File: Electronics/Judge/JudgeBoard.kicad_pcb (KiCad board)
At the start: 2 copper layers, 21 parts, among them J1 RJ12-UNSHLD, U1 74HC165, U2 74HC165

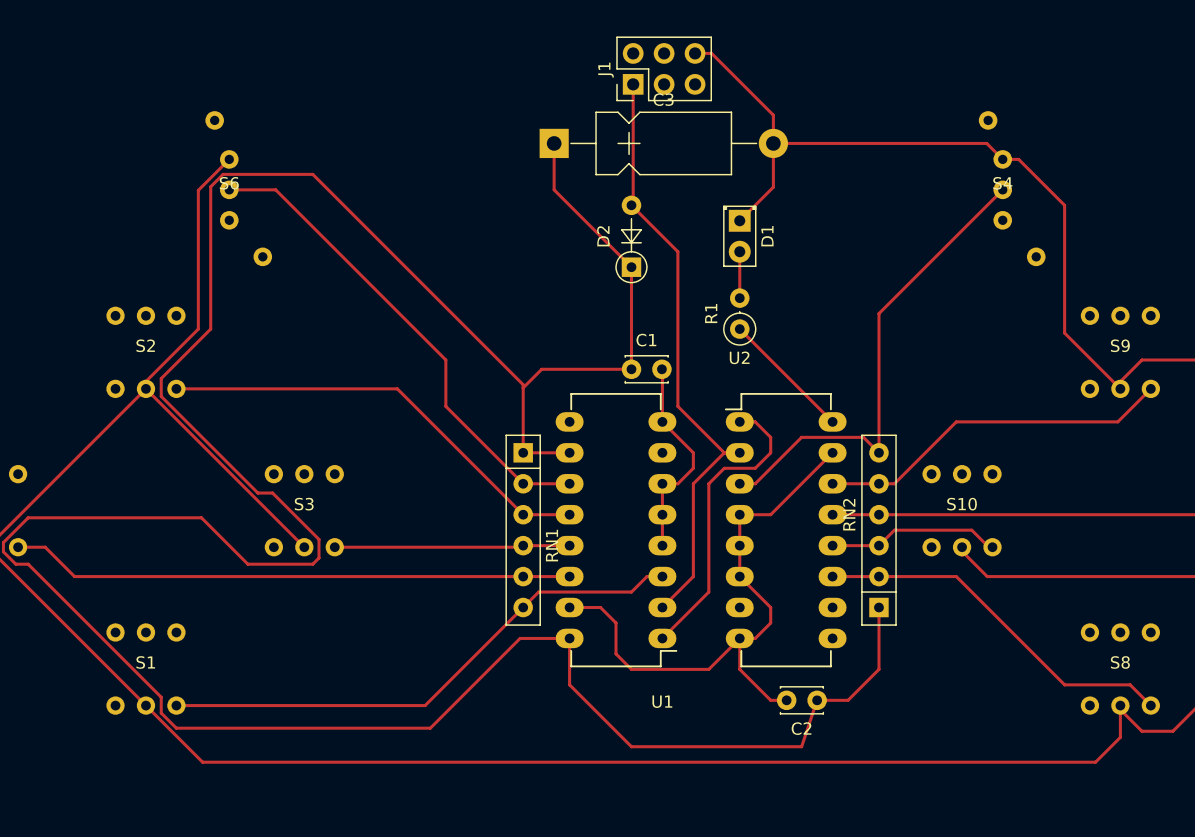
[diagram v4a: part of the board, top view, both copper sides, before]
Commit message: Reduced judge board to 2 jumpers
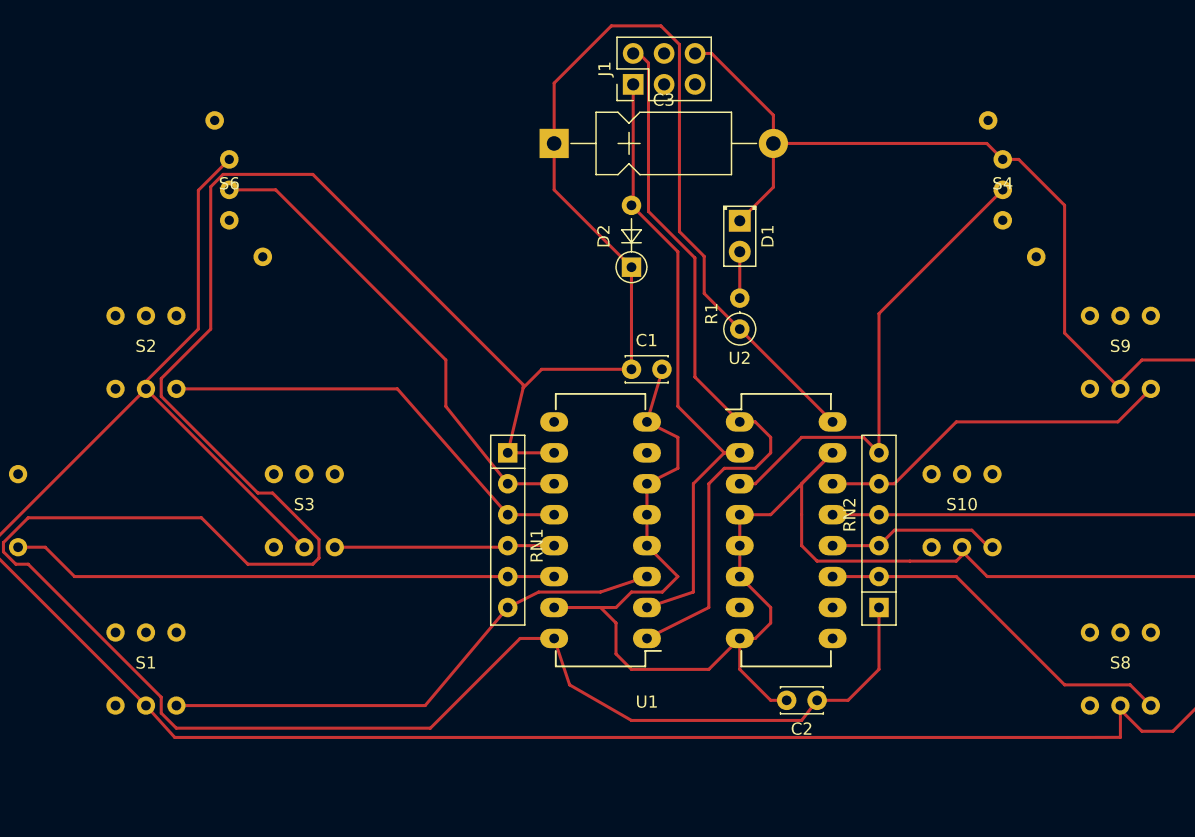
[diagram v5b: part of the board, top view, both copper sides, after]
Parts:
- moved RN1 1.27 mm to (139.7, 95.2)
- moved U1 1.27 mm to (151.1, 110.5)
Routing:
- net +3V3: track 248.1 -> 287.2 mm
- net /LOAD: track 24.7 -> 60.5 mm
- net GND: track 383.7 -> 418.1 mm
- net /CLK: track 50.8 -> 52.5 mm
- net Net-(RN1-Pad6): track 44.3 -> 42.9 mm
- net Net-(RN1-Pad5): track 46.3 -> 45.0 mm
- net Net-(RN1-Pad4): track 19.3 -> 18.1 mm
- net Net-(RN1-Pad3): track 36.6 -> 35.7 mm
- net Net-(RN1-Pad2): track 40.2 -> 39.3 mm

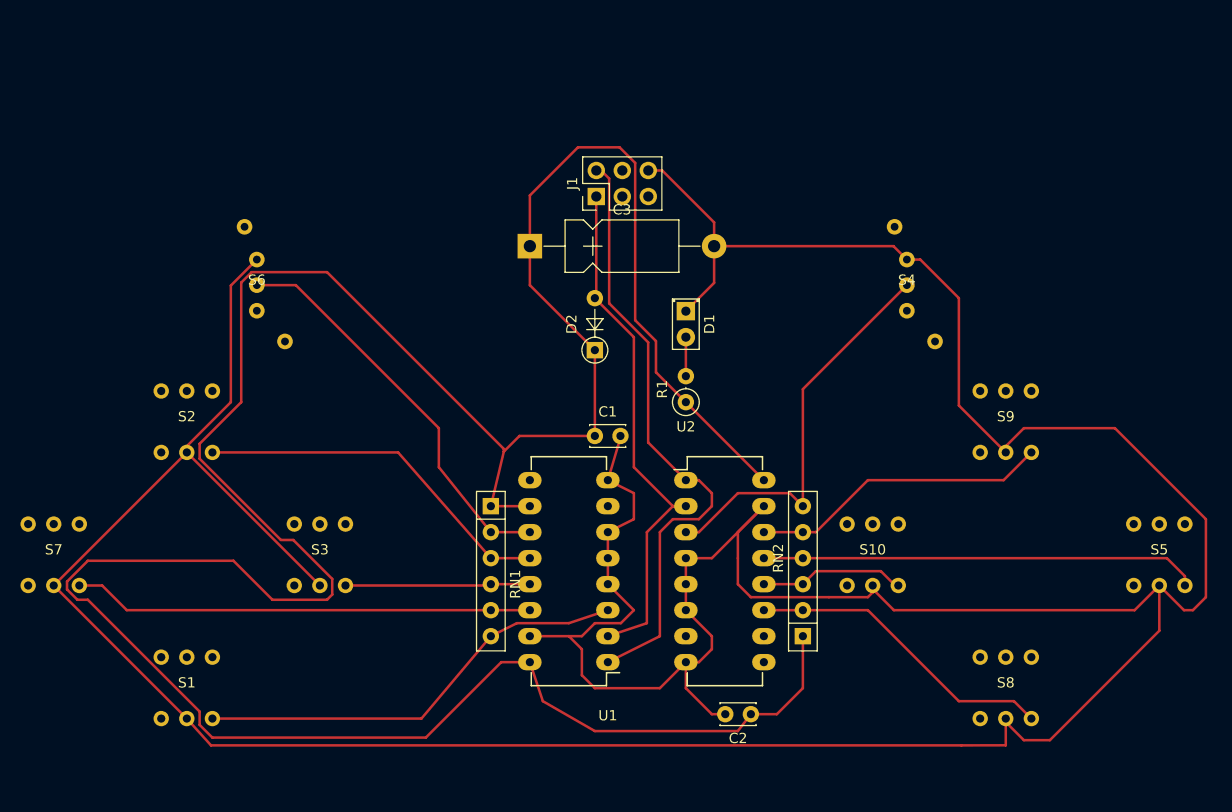
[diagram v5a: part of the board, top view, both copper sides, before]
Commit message: Cleaned up judge controller PCB, removed 3 jumpers
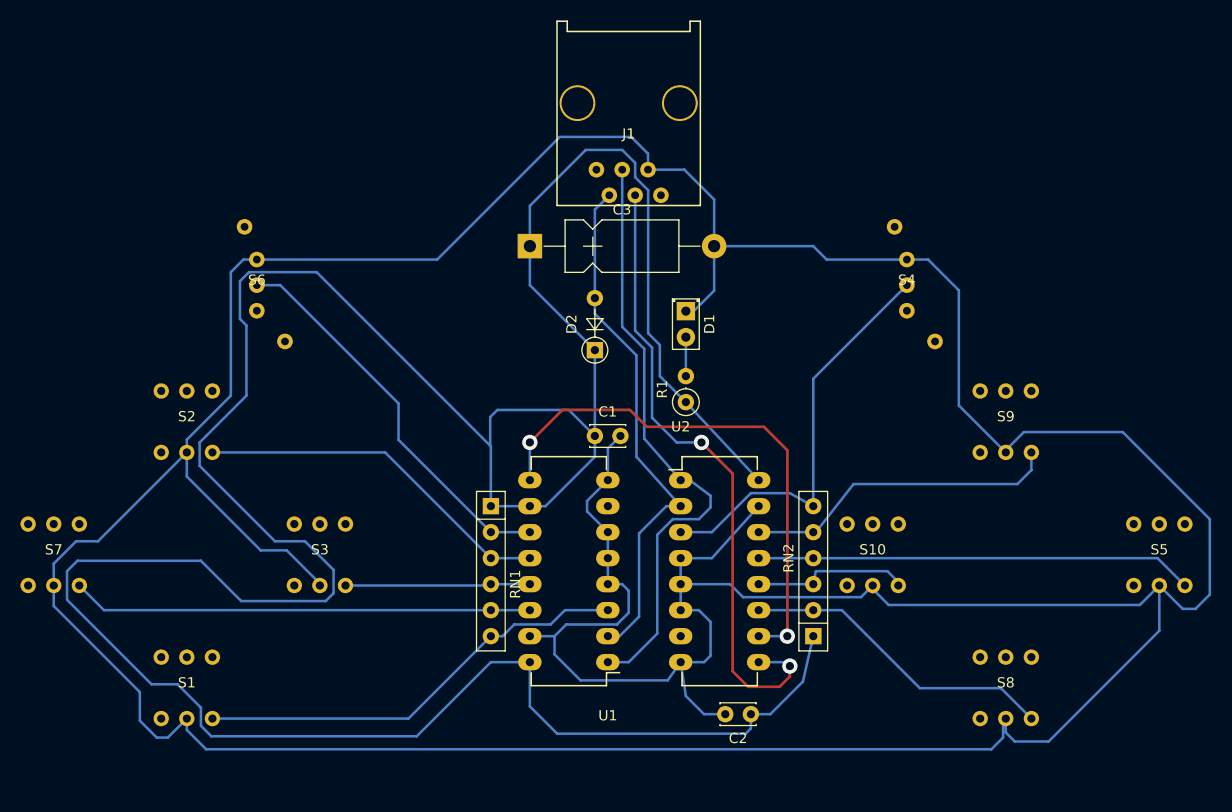
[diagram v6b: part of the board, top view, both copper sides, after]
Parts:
- J1: footprint Pin_Headers:Pin_Header_Straight_2x03_Pitch2.54mm -> PiKwonDo:TH-RJ12
- moved J1 9.65 mm to (153.2, 55.9), turned to 0 degrees
- moved RN2 1.02 mm to (171.2, 108.0)
- moved U2 0.51 mm to (158.2, 92.7)
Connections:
- J1 pad 1: /CLK -> (no net)
- J1 pad 2: /LOAD -> /CLK
- J1 pad 3: Net-(J1-Pad3) -> /LOAD
- J1 pad 4: (no net) -> Net-(J1-Pad4)
- J1 pad 5: (no net) -> GND
- J1 pad 6: GND -> (no net)
- U2 pad 9: Net-(J1-Pad3) -> Net-(J1-Pad4)
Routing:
- net Net-(J1-Pad4): track 0.00 -> 62.7 mm, vias 0 -> 2
- net GND: track 418.1 -> 473.8 mm
- net Net-(U1-Pad9): track 0.00 -> 52.7 mm, vias 0 -> 2
- net +3V3: track 287.2 -> 305.7 mm
- net Net-(RN2-Pad5): track 29.4 -> 31.2 mm
- net Net-(RN2-Pad3): track 14.2 -> 15.8 mm
- net /LOAD: track 60.5 -> 59.1 mm
- net Net-(RN2-Pad6): track 39.3 -> 40.2 mm
- net /CLK: track 52.5 -> 53.1 mm
- net Net-(RN1-Pad2): track 39.3 -> 38.7 mm
- net Net-(RN2-Pad2): track 30.5 -> 31.0 mm
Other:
- net class Default: via_dia 0.6 -> 1.5; via_drill 0.4 -> 0.8
